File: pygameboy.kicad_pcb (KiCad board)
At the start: 2 copper layers, 49.3 x 59.7 mm, 33 parts, among them J1 Conn_01x01, J2 Conn_01x01, J3 Conn_ARM_JTAG_SWD_10, J4 USB_B_Micro, Q1 BSS138, U1 CARTRIDGE, U2 SAMD51J, U3 74LS244, U4 74LS244, U5 74x4245, U6 74LS244, U7 AP2204K-3.3

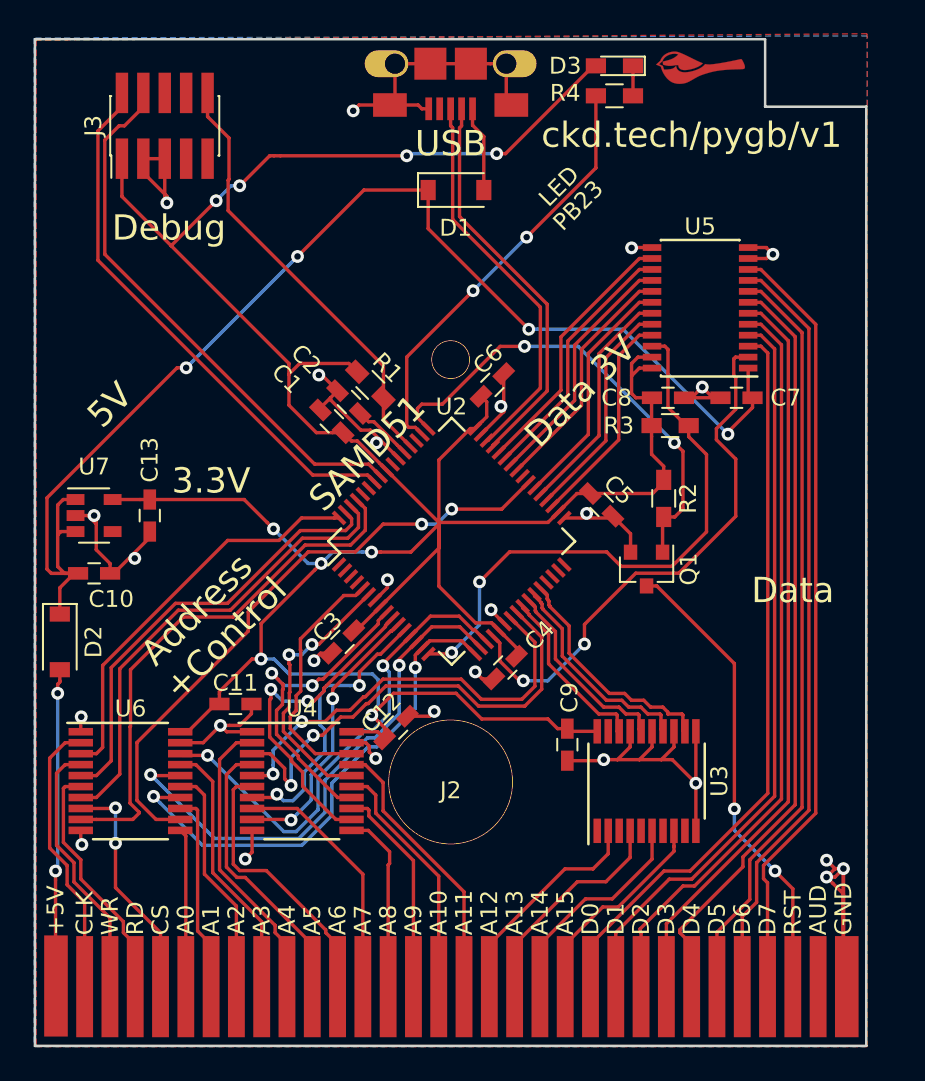
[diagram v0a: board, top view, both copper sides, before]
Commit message: v2 with added caps. reworked CCL signals and lotsa test points
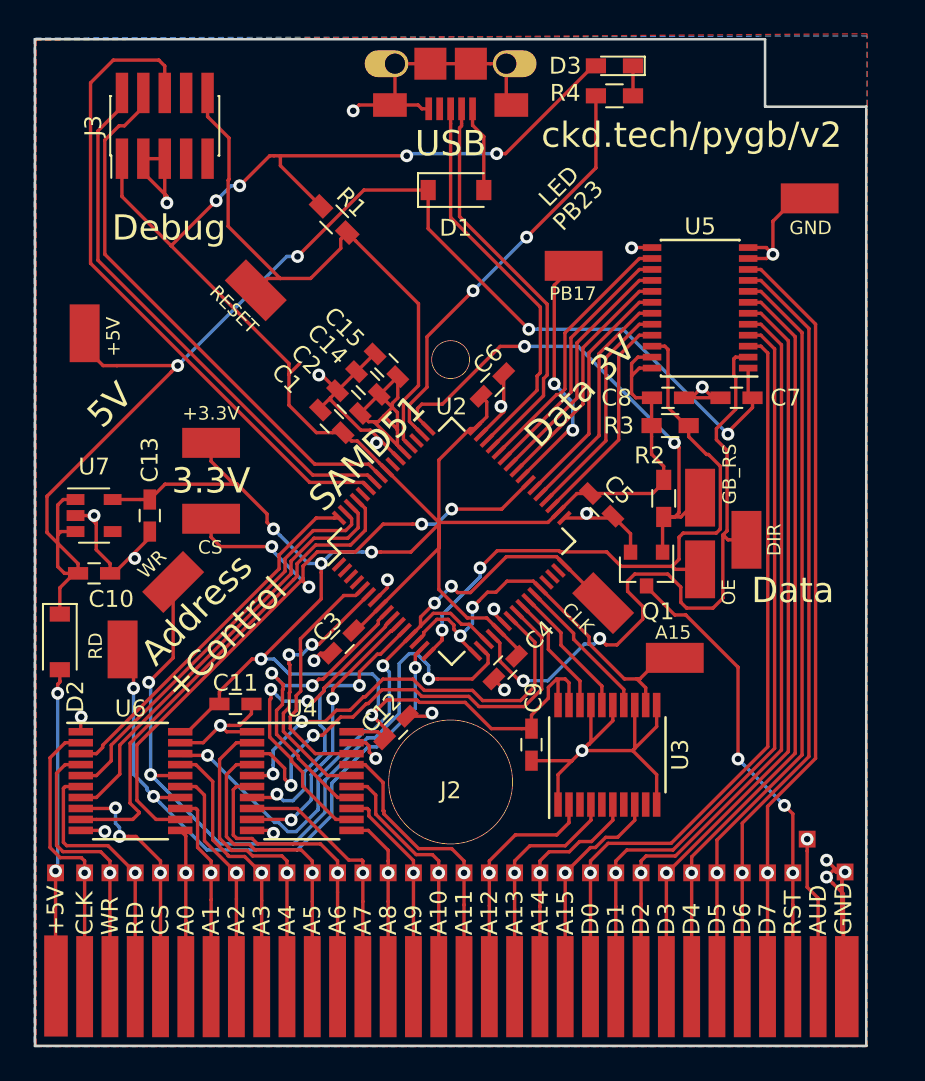
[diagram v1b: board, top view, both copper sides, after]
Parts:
- removed G***: LOGO, chickadee:chickadee_2mm_fcu
- added C14: 10uF, Capacitors_SMD:C_0603_HandSoldering, F.Cu at (119.7, 58.7)
- added C15: 1uF, Capacitors_SMD:C_0603_HandSoldering, F.Cu at (120.8, 57.6)
- added TP1: Test_Point, gameboy:Test Point, F.Cu at (101.2, 87.7)
- added TP10: Test_Point, gameboy:Test Point, F.Cu at (114.9, 87.7)
- added TP11: Test_Point, gameboy:Test Point, F.Cu at (116.4, 87.7)
- added TP12: Test_Point, gameboy:Test Point, F.Cu at (117.9, 87.7)
- added TP13: Test_Point, gameboy:Test Point, F.Cu at (119.4, 87.7)
- added TP14: Test_Point, gameboy:Test Point, F.Cu at (120.9, 87.7)
- added TP15: Test_Point, gameboy:Test Point, F.Cu at (122.4, 87.7)
- added TP16: Test_Point, gameboy:Test Point, F.Cu at (123.9, 87.7)
- added TP17: Test_Point, gameboy:Test Point, F.Cu at (125.4, 87.7)
- added TP18: Test_Point, gameboy:Test Point, F.Cu at (126.9, 87.7)
- added TP19: Test_Point, gameboy:Test Point, F.Cu at (128.4, 87.7)
- added TP2: Test_Point, gameboy:Test Point, F.Cu at (102.9, 87.7)
- added TP20: Test_Point, gameboy:Test Point, F.Cu at (129.9, 87.7)
- added TP21: Test_Point, gameboy:Test Point, F.Cu at (131.4, 87.7)
- added TP22: Test_Point, gameboy:Test Point, F.Cu at (132.9, 87.7)
- added TP23: Test_Point, gameboy:Test Point, F.Cu at (134.4, 87.7)
- added TP24: Test_Point, gameboy:Test Point, F.Cu at (135.9, 87.7)
- added TP25: Test_Point, gameboy:Test Point, F.Cu at (137.4, 87.7)
- added TP26: Test_Point, gameboy:Test Point, F.Cu at (138.9, 87.7)
- added TP27: Test_Point, gameboy:Test Point, F.Cu at (140.4, 87.7)
- added TP28: Test_Point, gameboy:Test Point, F.Cu at (141.9, 87.7)
- added TP29: Test_Point, gameboy:Test Point, F.Cu at (143.4, 87.7)
- added TP3: Test_Point, gameboy:Test Point, F.Cu at (104.4, 87.7)
- added TP30: Test_Point, gameboy:Test Point, F.Cu at (144.9, 87.7)
- added TP31: Test_Point, gameboy:Test Point, F.Cu at (145.8, 85.7)
- added TP32: Test_Point, gameboy:Test Point, F.Cu at (148.0, 87.7)
- added TP33: Test_Point, keystone:5015-SMT-TestPoint, F.Cu at (142.2, 68.0)
- added TP34: DATA_OE, keystone:5015-SMT-TestPoint, F.Cu at (139.4, 69.7)
- added TP35: GB_RESET, keystone:5015-SMT-TestPoint, F.Cu at (139.4, 65.5)
- added TP36: SAMD_RESET, keystone:5015-SMT-TestPoint, F.Cu at (113.1, 53.2)
- added TP37: gnd, keystone:5015-SMT-TestPoint, F.Cu at (145.9, 47.7)
- added TP38: 3.3v, keystone:5015-SMT-TestPoint, F.Cu at (110.4, 62.2)
- added TP39: batt, keystone:5015-SMT-TestPoint, F.Cu at (102.9, 55.7)
- added TP4: Test_Point, gameboy:Test Point, F.Cu at (105.9, 87.7)
- added TP40: clk, keystone:5015-SMT-TestPoint, F.Cu at (133.7, 71.7)
- added TP41: rd, keystone:5015-SMT-TestPoint, F.Cu at (105.2, 74.5)
- added TP42: wr, keystone:5015-SMT-TestPoint, F.Cu at (108.2, 70.5)
- added TP43: a15, keystone:5015-SMT-TestPoint, F.Cu at (137.9, 75.0)
- added TP44: PB17, keystone:5015-SMT-TestPoint, F.Cu at (131.9, 51.7)
- added TP45: cs, keystone:5015-SMT-TestPoint, F.Cu at (110.4, 66.7)
- added TP5: Test_Point, gameboy:Test Point, F.Cu at (107.4, 87.7)
- added TP6: Test_Point, gameboy:Test Point, F.Cu at (108.9, 87.7)
- added TP7: Test_Point, gameboy:Test Point, F.Cu at (110.4, 87.7)
- added TP8: Test_Point, gameboy:Test Point, F.Cu at (111.9, 87.7)
- added TP9: Test_Point, gameboy:Test Point, F.Cu at (113.4, 87.7)
- moved R1 10.0 mm to (117.7, 49.0)
- moved U3 2.80 mm to (133.9, 80.7)
- moved C9 2.13 mm to (129.4, 80.1)
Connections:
- J3 pad 6: Net-(J3-Pad6) -> /SWO
- U2 pad 14: /3V_WR -> /3V_A15
- U2 pad 17: /3V_RD -> /3V_A15
- U2 pad 32: Net-(U2-Pad32) -> /3V_CLK
- U2 pad 59: Net-(U2-Pad59) -> /SWO
- U3 pad 1: Net-(U3-Pad1) -> GND
- U3 pad 19: Net-(U3-Pad19) -> +3V3
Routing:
- net /SWO: track 0.00 -> 39.4 mm
- net Net-(TP44-Pad1): track 0.00 -> 14.8 mm, vias 0 -> 2
- net /3V_CLK: track 29.4 -> 43.9 mm, vias 2 -> 4
- net /3V_WR: track 31.7 -> 45.6 mm, vias 2 -> 3
- net Net-(C14-Pad2): track 3.59 -> 15.4 mm
- net GND: track 122.2 -> 133.6 mm, vias 26 -> 25
- net /3V_A15: track 13.9 -> 24.8 mm, vias 0 -> 2
- net Net-(TP31-Pad1): track 0.00 -> 9.02 mm, vias 0 -> 1
- net /SAMD_RESET: track 26.0 -> 35.0 mm
- net /3V_CS: track 36.8 -> 45.3 mm, vias 2 -> 4
- net /DIR: track 32.1 -> 40.0 mm
- net +3V3: track 182.6 -> 190.4 mm
- net /3V_RD: track 30.2 -> 36.3 mm, vias 2 -> 3
- net +5V: track 76.4 -> 82.4 mm
- net /3V_A14: track 12.7 -> 8.76 mm
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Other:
- board text added: "+3.3V"
- board text added: "DIR"
- board text added: "GB_RS"
- board text added: "OE"
- board text added: "PB17"
- board text added: "RESET"
- board text added: "ckd.tech/pygb/v2"
- board text removed: "ckd.tech/pygb/v1"

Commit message: v3
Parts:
- added C16: C_Small, Capacitor_SMD:C_0603_1608Metric_Pad1.05x0.95mm_HandSolder, F.Cu at (121.4, 56.1)
- added C17: C_Small, Capacitor_SMD:C_0603_1608Metric_Pad1.05x0.95mm_HandSolder, F.Cu at (113.1, 65.8)
- added D4: 1N4148W, Diode_SMD:D_SOD-123, F.Cu at (106.2, 54.2)
- added G***: LOGO, chickadee:chickadee_2mm_fcu, F.Cu at (146.0, 44.4)
- added J5: MIDI IN, cui-audio:CUI_SJ-3523-SMT-TR, F.Cu at (105.8, 45.3)
- added J6: MIDI OUT, cui-audio:CUI_SJ-3523-SMT-TR, F.Cu at (116.3, 45.3)
- added R5: R_Small, Resistor_SMD:R_0603_1608Metric_Pad1.05x0.95mm_HandSolder, F.Cu at (110.1, 53.3)
- added R6: R_Small, Resistor_SMD:R_0603_1608Metric_Pad1.05x0.95mm_HandSolder, F.Cu at (112.2, 53.5)
- added R7: R_Small, Resistor_SMD:R_0603_1608Metric_Pad1.05x0.95mm_HandSolder, F.Cu at (120.7, 46.8)
- added R8: 10k, Resistor_SMD:R_0603_1608Metric_Pad1.05x0.95mm_HandSolder, F.Cu at (109.3, 68.3)
- added TP46: data0, keystone:5015-SMT-TestPoint, F.Cu at (135.2, 64.6)
- added TP47: D0, keystone:5015-SMT-TestPoint, F.Cu at (142.2, 78.0)
- added U8: 6N137S, Package_DIP:SMDIP-8_W9.53mm, F.Cu at (106.6, 61.4)
- moved J3 31.5 mm to (139.2, 43.5), turned to 270 degrees
- moved TP39 14.1 mm to (101.5, 69.7)
- moved TP36 9.02 mm to (122.1, 54.0)
- moved R1 4.92 mm to (122.3, 50.9)
- moved U7 4.72 mm to (104.7, 71.1)
- moved C13 4.56 mm to (107.5, 71.1)
- moved C10 4.11 mm to (104.7, 73.9)
- moved TP38 3.60 mm to (113.8, 60.8), turned to 270 degrees
- moved TP45 3.37 mm to (112.2, 69.6), turned to 45 degrees
- moved TP42 3.27 mm to (108.7, 73.7)
- moved TP41 2.37 mm to (104.4, 76.7)
- moved D3 1.82 mm to (132.7, 40.6), turned to 270 degrees
- moved J4 1.76 mm to (126.4, 39.6)
- moved D1 1.47 mm to (126.4, 46.9)
- moved C5 1.43 mm to (133.3, 67.3), turned to 90 degrees
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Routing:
- net GND: track 133.6 -> 110.9 mm, vias 25 -> 23
- net Net-(D4-Pad2): track 0.00 -> 16.5 mm
- net Net-(J5-PadT): track 0.00 -> 8.93 mm, vias 0 -> 2
- net +3V3: track 190.4 -> 184.0 mm
- net /SAMD_RESET: track 35.0 -> 28.6 mm, vias 0 -> 2
- net /SWO: track 39.4 -> 34.0 mm, vias 0 -> 4
- net Net-(D4-Pad1): track 0.00 -> 4.72 mm
- net /MIDI_IN: track 0.00 -> 4.70 mm
- net Net-(J6-PadR): track 0.00 -> 3.58 mm
- net /3V_WR: track 45.6 -> 42.6 mm
- net /3V_D0: track 13.0 -> 15.8 mm
- net Net-(J6-PadT): track 0.00 -> 2.64 mm
- net +5V: track 82.4 -> 79.8 mm
- net /SWDIO: track 32.4 -> 34.9 mm, vias 0 -> 2
- net /SHIELD: track 0.00 -> 2.19 mm, vias 0 -> 1
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- added copper zone on B.Cu, net /SHIELD
- added copper zone on F.Cu, net /SHIELD
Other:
- board text added: "Address"
- board text added: "IN"
- board text added: "OUT"
- board text added: "ckd.tech/pygb/v3"
- board text removed: "3.3V"
- board text removed: "5V"
- board text removed: "Address +Control"
- board text removed: "ckd.tech/pygb/v2"

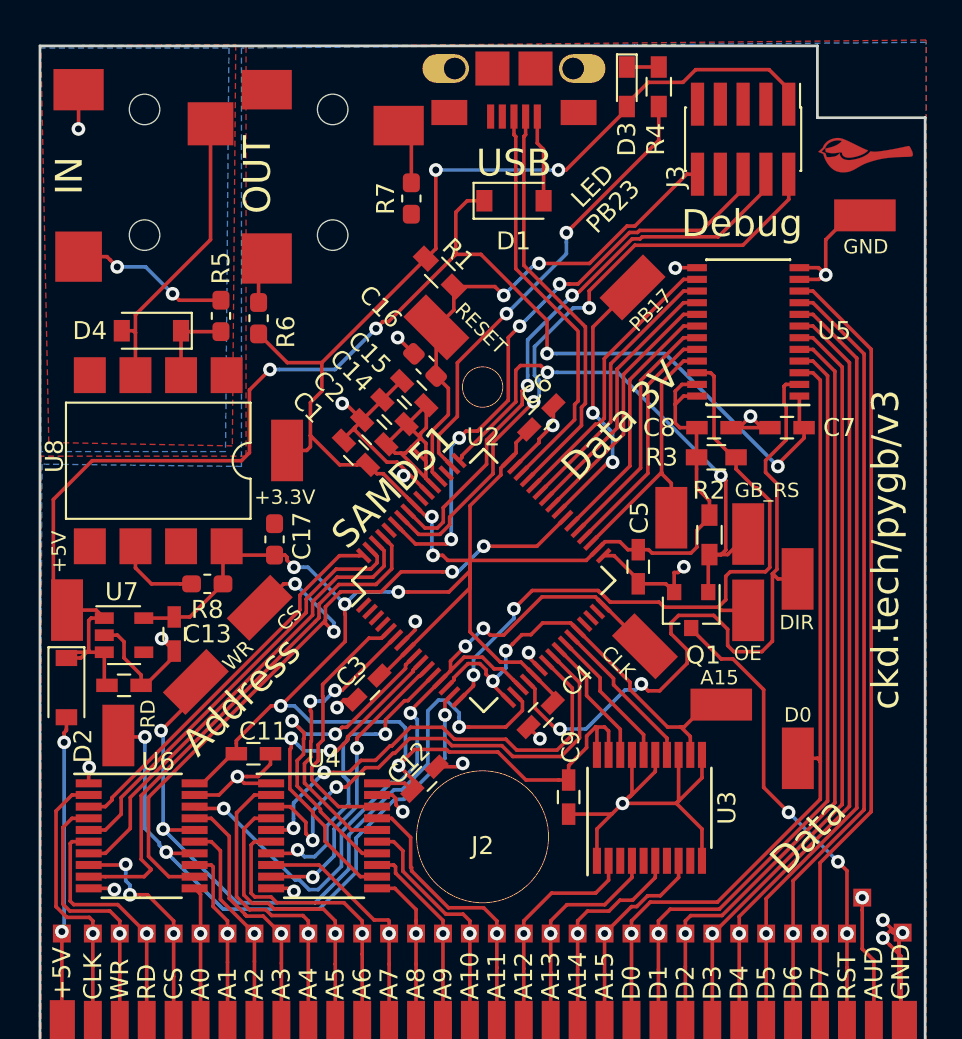
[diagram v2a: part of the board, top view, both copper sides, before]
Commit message: Fixup MIDI and switch to Adafruit parts
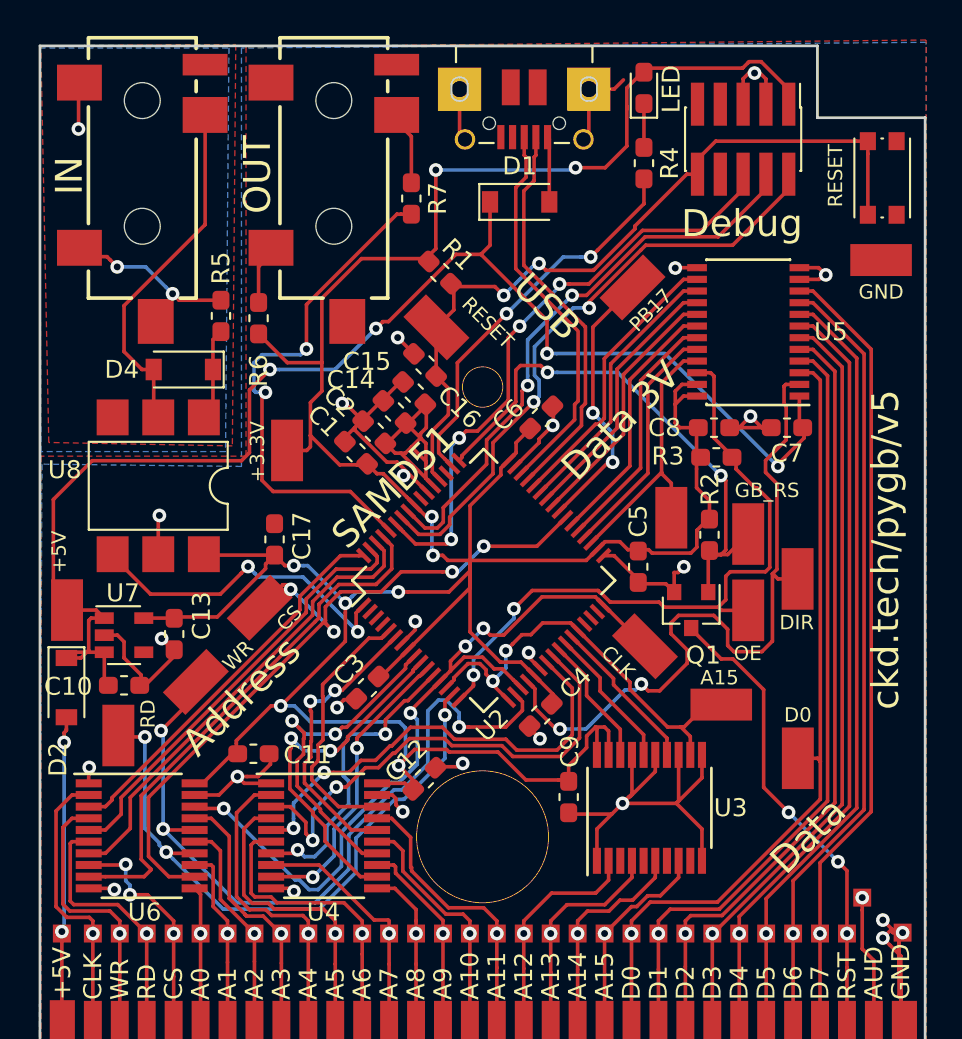
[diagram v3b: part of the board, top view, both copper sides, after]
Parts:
- removed G***: LOGO, chickadee:chickadee_2mm_fcu
- removed R8: 10k, Resistor_SMD:R_0603_1608Metric_Pad1.05x0.95mm_HandSolder
- added SW1: SW_Push, Button_Switch_SMD:SW_SPST_KMR2, F.Cu at (146.9, 45.7)
- C1, C10, C11, C12, C13, C14, C15, C2, C3, C4, C5, C6, C7, C8, C9: footprint Capacitors_SMD:C_0603_HandSoldering -> Capacitor_SMD:C_0603_1608Metric_Pad1.05x0.95mm_HandSolder
- D1, D2: footprint Diodes_SMD:D_SOD-123 -> Diode_SMD:D_SOD-123
- D3: footprint LEDs:LED_0603_HandSoldering -> LED_SMD:LED_0603_1608Metric_Pad1.05x0.95mm_HandSolder
- J4: footprint fci:Mini-USB-B-OshPark -> adafruit:4UCONN_20329_V2_USB
- J5, J6: footprint cui-audio:CUI_SJ-3523-SMT-TR -> adafruit:4UCONN_19269_TRS
- R1, R2, R3, R4: footprint Resistors_SMD:R_0603_HandSoldering -> Resistor_SMD:R_0603_1608Metric_Pad1.05x0.95mm_HandSolder
- R5: value R_Small -> 220
- R6, R7: value R_Small -> 51
- U2: footprint Housings_QFP:LQFP-64_10x10mm_Pitch0.5mm -> Package_QFP:LQFP-64_10x10mm_P0.5mm
- U3, U4, U6: footprint Housings_SSOP:TSSOP-20_4.4x6.5mm_Pitch0.65mm -> Package_SO:TSSOP-20_4.4x6.5mm_P0.65mm
- U5: footprint Housings_SSOP:TSSOP-24_4.4x7.8mm_Pitch0.65mm -> Package_SO:TSSOP-24_4.4x7.8mm_P0.65mm
- U7: footprint TO_SOT_Packages_SMD:SOT-23-5 -> Package_TO_SOT_SMD:SOT-23-5
- U8: value 6N137S -> H11L1; footprint Package_DIP:SMDIP-8_W9.53mm -> Package_DIP:SMDIP-6_W7.62mm
- moved J5 7.49 mm to (105.7, 37.8)
- moved J6 7.49 mm to (116.4, 37.8)
- moved R4 4.33 mm to (133.6, 44.8)
- moved J4 3.10 mm to (127.0, 42.6)
- moved D4 2.80 mm to (108.0, 56.3)
- moved TP37 2.65 mm to (146.8, 50.2)
- moved U8 1.40 mm to (106.6, 62.8)
- moved D3 0.95 mm to (133.6, 40.6), turned to 90 degrees
- moved D1 0.32 mm to (126.7, 47.0)
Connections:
- U2 pad 1: Net-(U2-Pad1) -> /MIDI_IN
- U2 pad 60: Net-(U2-Pad60) -> /MIDI_OUT
- U8 pad 1: Net-(U8-Pad1) -> Net-(D4-Pad1)
- U8 pad 2: Net-(D4-Pad1) -> Net-(D4-Pad2)
- U8 pad 3: Net-(D4-Pad2) -> Net-(U8-Pad3)
- U8 pad 4: Net-(U8-Pad4) -> /MIDI_IN
- U8 pad 6: /MIDI_IN -> +3V3
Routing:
- net /MIDI_OUT: track 0.00 -> 29.1 mm, vias 0 -> 2
- net /SAMD_RESET: track 28.6 -> 43.8 mm
- net /MIDI_IN: track 4.70 -> 18.5 mm, vias 0 -> 2
- net GND: track 110.9 -> 120.7 mm, vias 23 -> 25
- net +3V3: track 184.0 -> 190.9 mm
- net /LED: track 25.5 -> 21.8 mm
- net Net-(D4-Pad2): track 16.5 -> 19.9 mm
- net VBUS: track 4.84 -> 3.65 mm
- net +5V: track 79.8 -> 78.7 mm
- net /USB_D+: track 22.6 -> 21.7 mm
- net /USB_D-: track 23.0 -> 22.1 mm
- net /SWDIO: track 34.9 -> 34.2 mm
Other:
- board text added: "LED"
- board text added: "ckd.tech/pygb/v5"
- board text removed: "LED PB23"
- board text removed: "ckd.tech/pygb/v3"

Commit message: More work on v5
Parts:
- added G***: LOGO, chickadee:chickadee_6mm, B.Cu at (140.4, 46.0)
- added R8: 470, Resistor_SMD:R_0603_1608Metric_Pad1.05x0.95mm_HandSolder, F.Cu at (111.5, 66.2)
- C14: footprint Capacitor_SMD:C_0603_1608Metric_Pad1.05x0.95mm_HandSolder -> Capacitor_SMD:C_0805_2012Metric_Pad1.15x1.40mm_HandSolder
- D3: footprint LED_SMD:LED_0603_1608Metric_Pad1.05x0.95mm_HandSolder -> LED_SMD:LED_0805_2012Metric_Pad1.15x1.40mm_HandSolder
- U2: footprint Package_QFP:LQFP-64_10x10mm_P0.5mm -> Package_DFN_QFN:QFN-64-1EP_9x9mm_P0.5mm_EP4.7x4.7mm_ThermalVias
- U3, U4, U6: value 74LS244 -> 74LVC244
- moved C1 0.68 mm to (117.1, 61.4)
- moved C2 0.32 mm to (118.4, 60.1)
- moved U2 0.20 mm to (124.7, 68.3)
- moved C14 0.18 mm to (119.6, 58.7)
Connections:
- U4 pad 12: /3V_A7 -> /3V_A4
- U4 pad 14: /3V_A6 -> /3V_A5
- U4 pad 16: /3V_A5 -> /3V_A6
- U4 pad 18: /3V_A4 -> /3V_A7
- U4 pad 2: /A4 -> /A7
- U4 pad 4: /A5 -> /A6
- U4 pad 6: /A6 -> /A5
- U4 pad 8: /A7 -> /A4
- U6 pad 11: /A0 -> /A3
- U6 pad 13: /A1 -> /A2
- U6 pad 15: /A2 -> /A1
- U6 pad 17: /A3 -> /A0
- U6 pad 3: /3V_A3 -> /3V_A0
- U6 pad 5: /3V_A2 -> /3V_A1
- U6 pad 7: /3V_A1 -> /3V_A2
- U6 pad 9: /3V_A0 -> /3V_A3
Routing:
- net GND: track 120.7 -> 136.6 mm, vias 25 -> 24
- net /A0: track 9.40 -> 17.1 mm
- net /3V_A7: track 20.0 -> 14.5 mm, vias 2 -> 0
- net /3V_A0: track 29.6 -> 24.2 mm
- net /3V_A3: track 21.6 -> 27.0 mm
- net /A4: track 19.0 -> 13.7 mm
- net /A1: track 11.9 -> 17.0 mm
- net /3V_A4: track 14.8 -> 19.8 mm
- net /A5: track 18.6 -> 14.4 mm
- net /3V_CLK: track 43.9 -> 39.7 mm, vias 4 -> 2
- net /A3: track 16.3 -> 12.6 mm
- net /SWDIO: track 34.2 -> 37.7 mm, vias 2 -> 4
- net /3V_A6: track 19.2 -> 15.9 mm, vias 2 -> 0
- net /SWCLK: track 32.2 -> 35.4 mm, vias 2 -> 4
- net /A7: track 15.3 -> 18.1 mm
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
